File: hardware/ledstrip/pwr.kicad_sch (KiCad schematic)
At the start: 8 parts, among them J4 BMS connectors, J6 Header for STUSB4500 I2C, U5 BQ25703A, U6 STUSB4500QTR

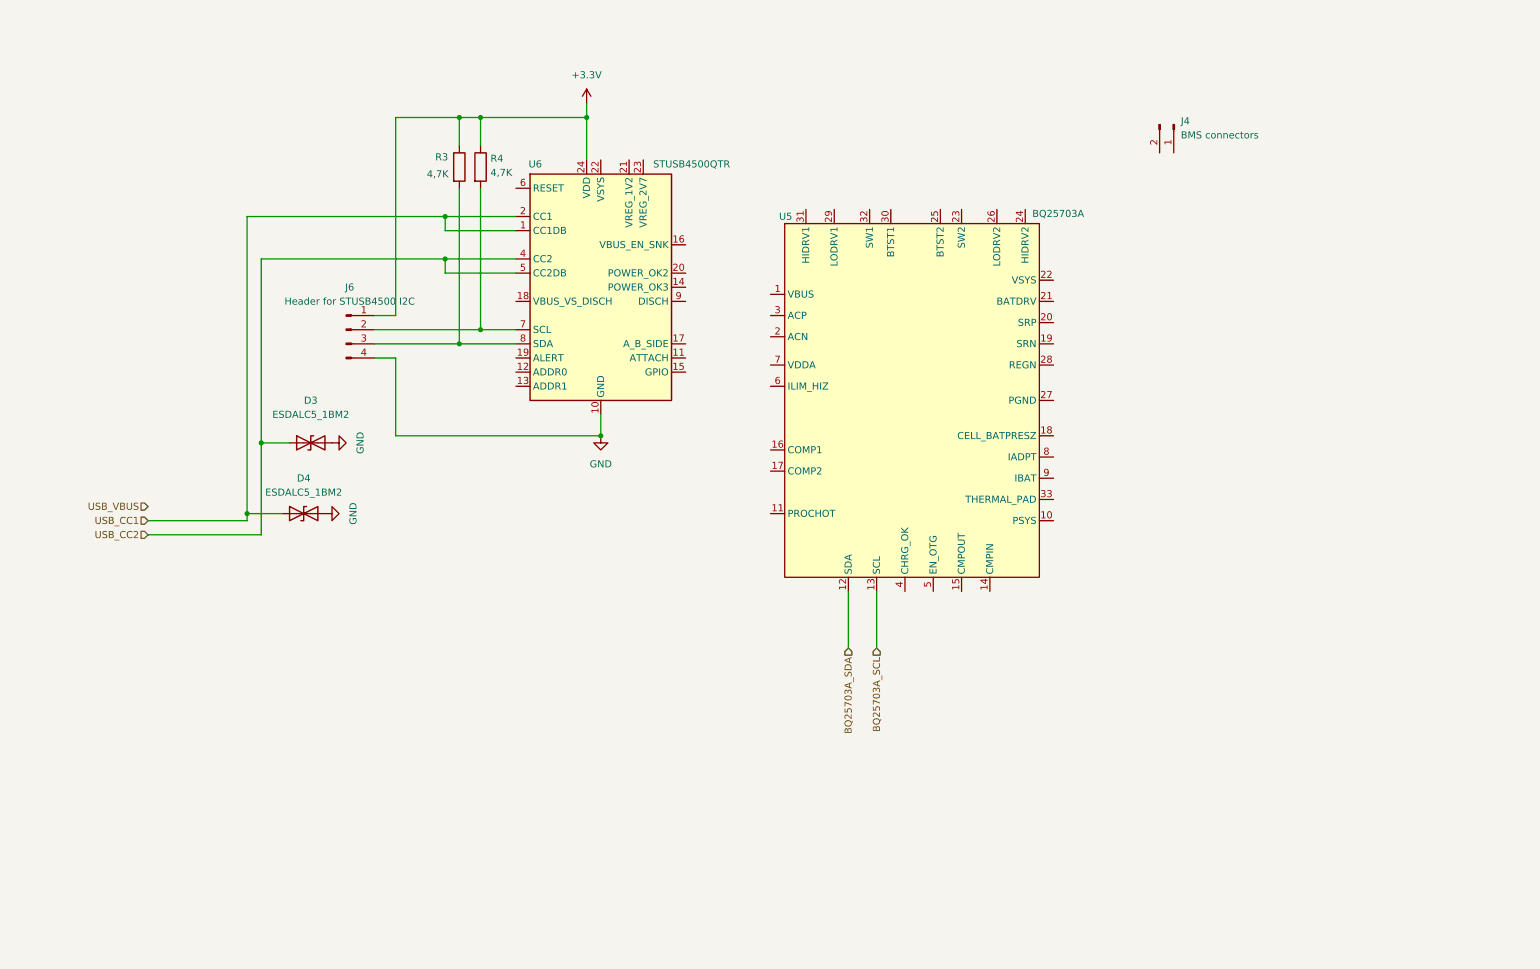
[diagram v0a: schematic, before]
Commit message: Add TVS diode on VBUS line, improve STUSB4500 integration
Add P-MOSFET controled by STUSB4500 on VBUS line
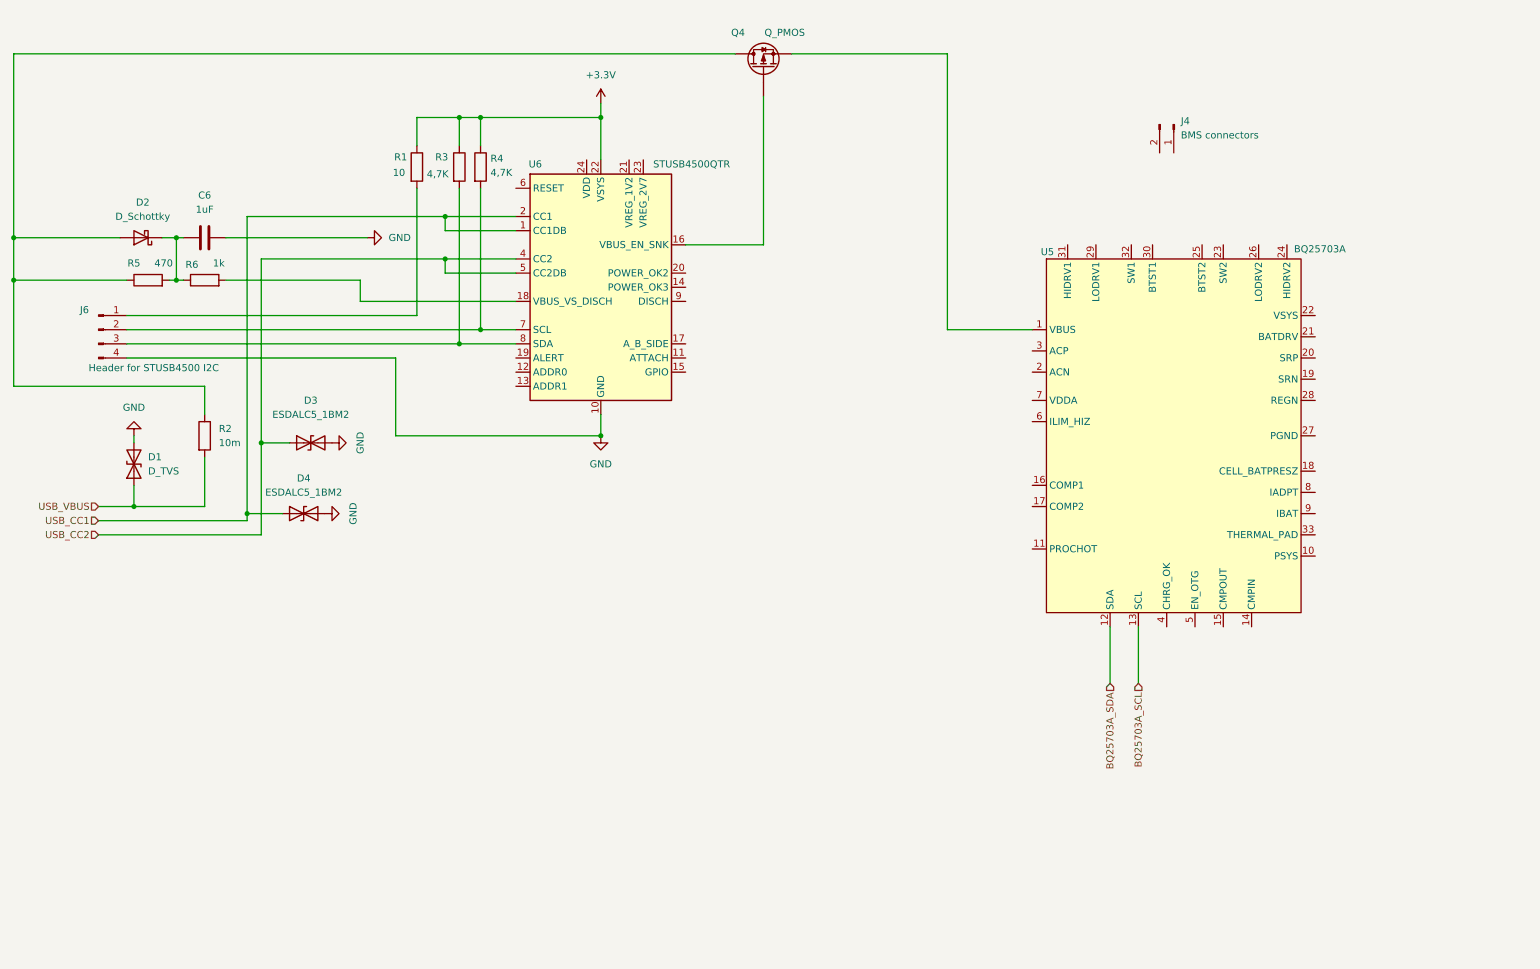
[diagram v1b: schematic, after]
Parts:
- added C6: 1uF, Capacitor_SMD:C_0603_1608Metric, symbol Device:C
- added D1: D_TVS, Diode_SMD:D_SMA, symbol Device:D_TVS
- added D2: D_Schottky, Diode_SMD:D_SOD-323, symbol Device:D_Schottky
- added Q4: Q_PMOS, symbol Device:Q_PMOS
- added R1: 10, Resistor_SMD:R_0805_2012Metric, symbol Device:R
- added R2: 10m, Resistor_SMD:R_0805_2012Metric, symbol Device:R
- added R5: 470, Capacitor_SMD:C_0603_1608Metric, symbol Device:R
- added R6: 1k, Capacitor_SMD:C_0603_1608Metric, symbol Device:R
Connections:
- net +3.3V: now also U6.22 (VSYS), R1.1; no longer J6.1 (Pin_1), U6.24 (VDD)
- net GND: now also C6.2, D1.2 (A2)
- net USB_VBUS: now also D1.1 (A1), R2.2
- net at U6.16 (VBUS_EN_SNK): now also Q4.G
- net at U6.18 (VBUS_VS_DISCH): now also R6.2
- net at U5.1 (VBUS): now also Q4.S
- new net: C6.1, D2.1 (K), R5.2, R6.1
- new net: J6.1 (Pin_1), R1.2
- new net: D2.2 (A), Q4.D, R2.1, R5.1
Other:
- moved on the sheet: J6, U5

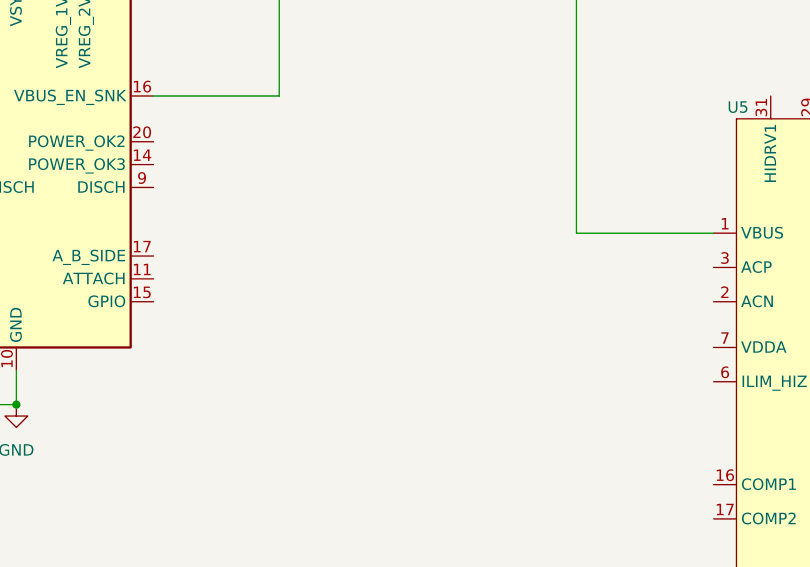
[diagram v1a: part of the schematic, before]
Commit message: Add STL6P3LLH6 sym from ulra librarian, add a TODO_plan_for_this_weekend.md for project organization
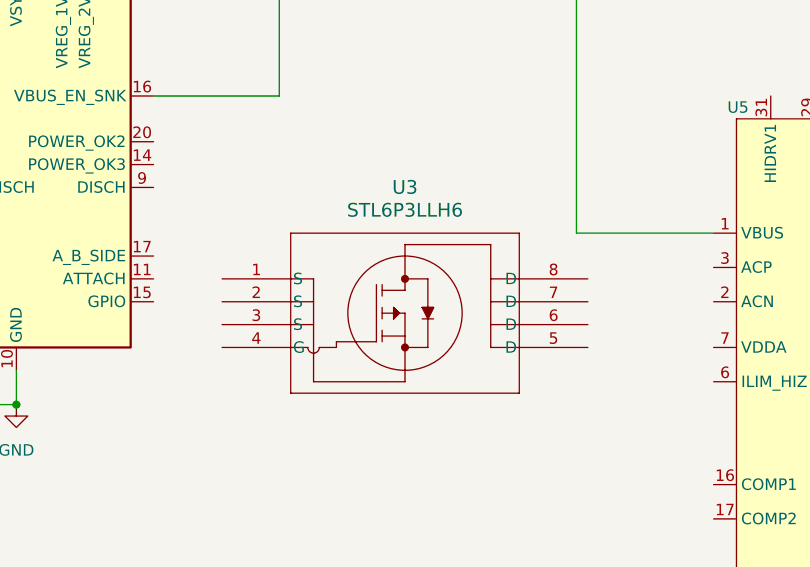
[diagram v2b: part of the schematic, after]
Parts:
- added U3: STL6P3LLH6, POWERFLAT_3P3X3P3_STM, symbol STL6P3LLH6:STL6P3LLH6
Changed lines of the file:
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@@
+	)
+	(symbol
+		(lib_id "STL6P3LLH6:STL6P3LLH6")
+		(at 142.24 72.39 0)
+		(unit 1)
+		(exclude_from_sim no)
+		(in_bom yes)
+		(on_board yes)
+		(dnp no)
+		(fields_autoplaced yes)
+		(property "Reference" "U3"
+			(at 162.56 62.23 0)
+			(effects
+				(font
+					(size 1.524 1.524)
+				)
+			)
+		)
+		(property "Value" "STL6P3LLH6"
+			(at 162.56 64.77 0)
+			(effects
+				(font
+					(size 1.524 1.524)
+				)
+			)
+		)
+		(property "Footprint" "POWERFLAT_3P3X3P3_STM"
+			(at 142.24 72.39 0)
+			(effects
+				(font
+					(size 1.27 1.27)
+					(italic yes)
+				)
+				(hide yes)
+			)
+		)
+		(property "Datasheet" "https://www.st.com/resource/en/datasheet/stl6p3llh6.pdf"
+			(at 142.24 72.39 0)
+			(effects
+				(font
+					(size 1.27 1.27)
+					(italic yes)
+				)
+				(hide yes)
+			)
+		)
+		(property "Description" ""
+			(at 142.24 72.39 0)
+			(effects
+				(font
+					(size 1.27 1.27)
+				)
+				(hide yes)
+			)
+		)
+		(pin "5"
+		)
+		(pin "6"
+		)
+		(pin "7"
+		)
+		(pin "8"
+		)
+		(pin "3"
+		)
+		(pin "2"
+		)
+		(pin "1"
+		)
+		(pin "4"
+		)
+		(instances
+			(project ""
+				(path "/dcb997ee-94c4-4df2-ba22-0e091735ddd7/b5cca531-fcff-4497-988a-ecdd56b3ddf9"
+					(reference "U3")
+					(unit 1)
+				)
+			)
+		)
 	)
 	(symbol

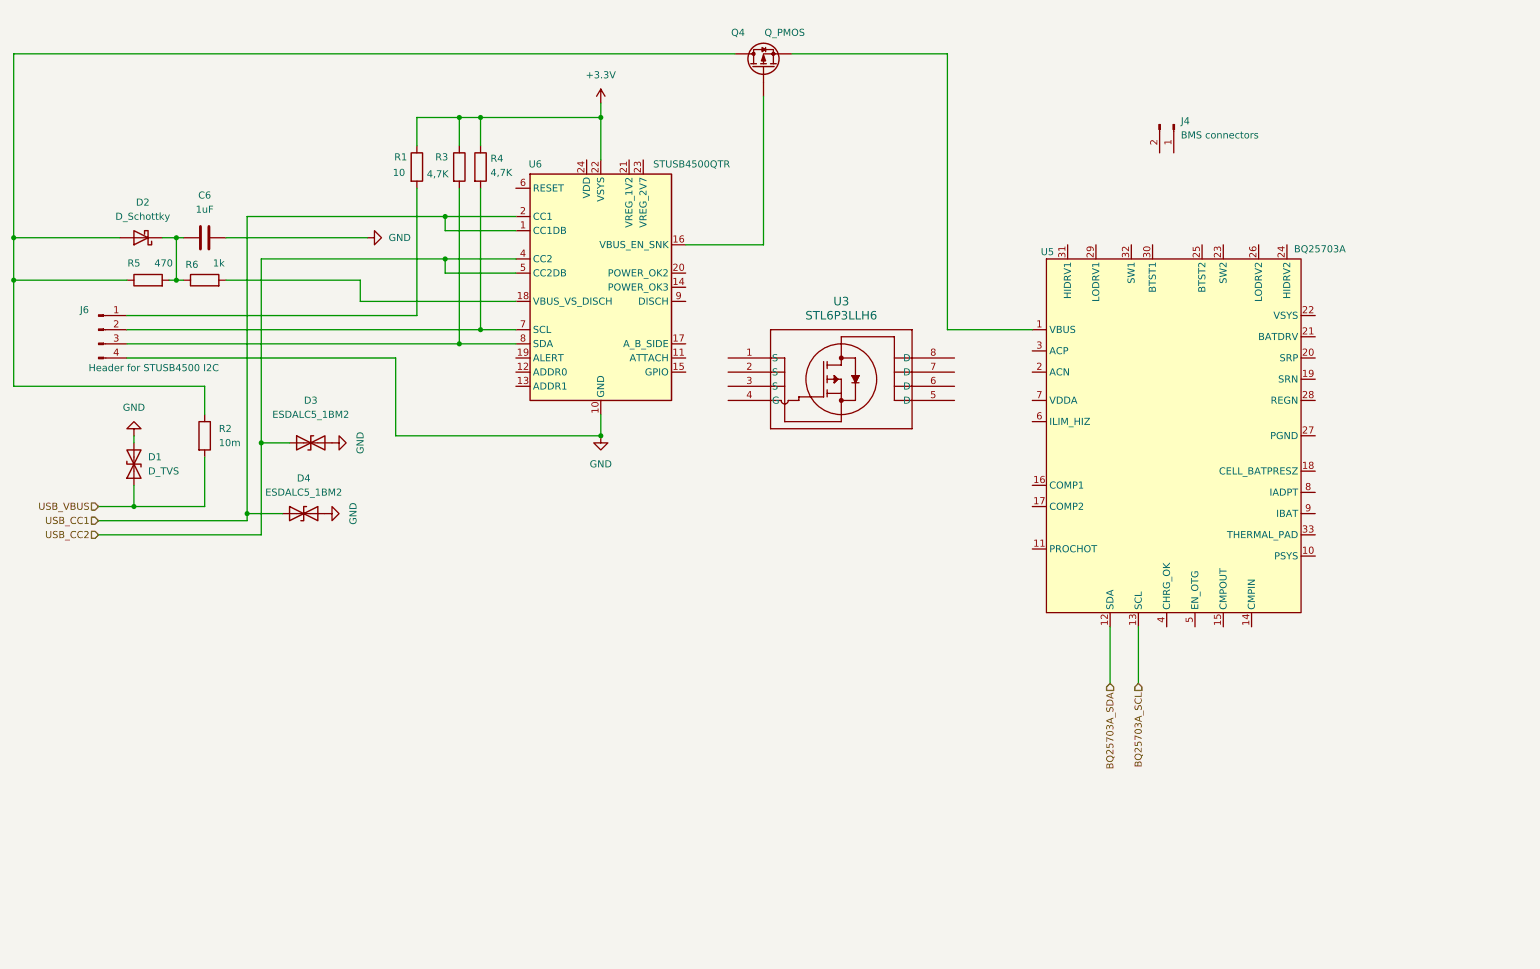
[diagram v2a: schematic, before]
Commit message: Finished STUSB4500 integration.
Improved BQ25703A integration.
Created a footprint for Wurth inductance.
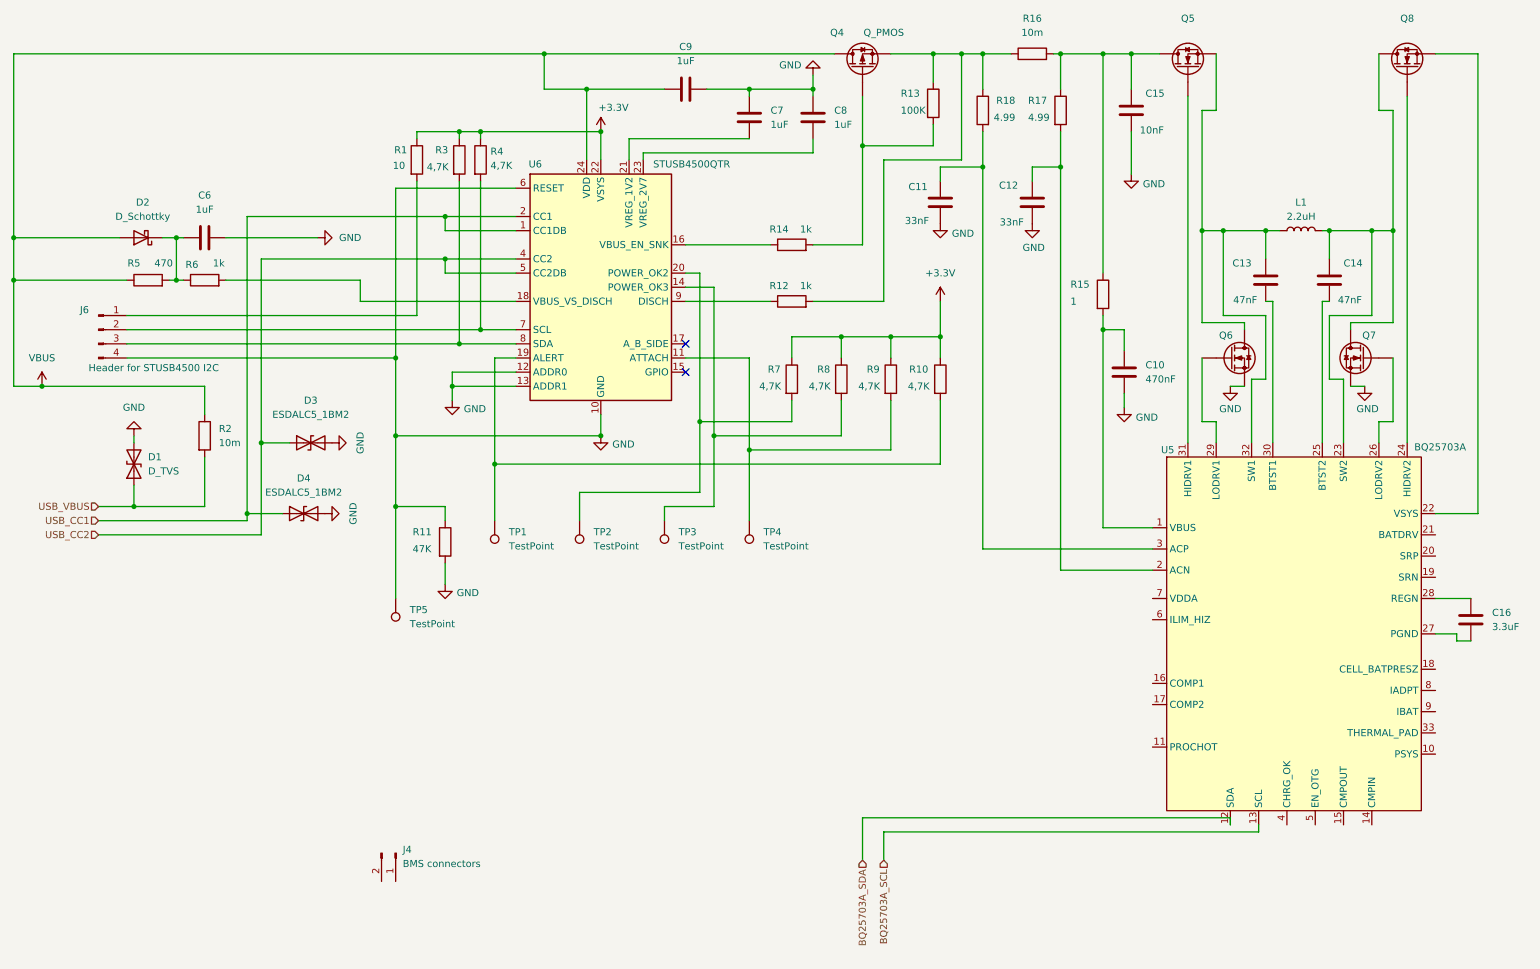
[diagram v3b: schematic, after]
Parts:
- removed U3: STL6P3LLH6, POWERFLAT_3P3X3P3_STM, symbol STL6P3LLH6:STL6P3LLH6
- added C10: 470nF, Capacitor_SMD:C_0603_1608Metric, symbol Device:C
- added C11, C12: 33nF, Capacitor_SMD:C_0603_1608Metric, symbol Device:C
- added C13, C14: 47nF, Capacitor_SMD:C_0603_1608Metric, symbol Device:C
- added C15: 10nF, Capacitor_SMD:C_0603_1608Metric, symbol Device:C
- added C16: 3.3uF, Capacitor_SMD:C_0603_1608Metric, symbol Device:C
- added C7, C8, C9: 1uF, Capacitor_SMD:C_0603_1608Metric, symbol Device:C
- added L1: 2.2uH, ledstrip:L_Wurth_WE-LHMI-8030_9.7x8.5mm, symbol Device:L
- added Q5, Q6, Q7, Q8: Q_NMOS, Package_SON:VSON-8_3.3x3.3mm_P0.65mm_NexFET, symbol Device:Q_NMOS
- added R10, R7, R8, R9: 4,7K, Resistor_SMD:R_0805_2012Metric, symbol Device:R
- added R11: 47K, Resistor_SMD:R_0805_2012Metric, symbol Device:R
- added R12, R14: 1k, Capacitor_SMD:C_0603_1608Metric, symbol Device:R
- added R13: 100K, Resistor_SMD:R_0805_2012Metric, symbol Device:R
- added R15: 1, Resistor_SMD:R_0805_2012Metric, symbol Device:R
- added R16: 10m, Resistor_SMD:R_0805_2012Metric, symbol Device:R
- added R17, R18: 4.99, Resistor_SMD:R_0805_2012Metric, symbol Device:R
- added TP1, TP2, TP3, TP4, TP5: TestPoint, symbol Connector:TestPoint
- Q4: footprint (none) -> STL6P3LLH6:POWERFLAT_3P3X3P3_STM
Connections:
- net +3.3V: now also R10.1, R7.1, R8.1, R9.1
- net GND: now also U6.12 (ADDR0), U6.13 (ADDR1), U6.6 (RESET), C10.1, C11.1, C12.1, C15.1, C7.2, C8.2, C9.2, Q6.S, Q7.S, R11.1, R11.2, TP5.1
- net VBUS: now reaches D2.2 (A), Q4.D, R2.1, R5.1
- net VBUS: now also U6.24 (VDD), C9.1
- net at Q4.G: now also R13.2, R14.2; no longer U6.16 (VBUS_EN_SNK)
- net at Q4.S: now also R12.2, R13.1, R16.1, R18.1; no longer U5.1 (VBUS)
- net at U6.11 (ATTACH): now also R9.2, TP4.1
- net at U6.14 (POWER_OK3): now also R8.2, TP3.1
- net at U6.19 (ALERT): now also R10.2, TP1.1
- net at U6.20 (POWER_OK2): now also R7.2, TP2.1
- net at U6.21 (VREG_1V2): now also C7.1
- net at U6.23 (VREG_2V7): now also C8.1
- net at U6.9 (DISCH): now also R12.1
- net at U5.2 (ACN): now also C12.2, R17.2
- net at U5.22 (VSYS): now also Q8.S
- net at U5.23 (SW2): now also C14.2, L1.2, Q7.D, Q8.D
- net at U5.24 (HIDRV2): now also Q8.G
- net at U5.25 (BTST2): now also C14.1
- net at U5.26 (LODRV2): now also Q7.G
- net at U5.27 (PGND): now also C16.1
- net at U5.28 (REGN): now also C16.2
- net at U5.29 (LODRV1): now also Q6.G
- net at U5.3 (ACP): now also C11.2, R18.2
- net at U5.30 (BTST1): now also C13.1
- net at U5.31 (HIDRV1): now also Q5.G
- net at U5.32 (SW1): now also C13.2, L1.1, Q5.S, Q6.D
- new net: C15.2, Q5.D, R15.1, R16.2, R17.1
- new net: C10.2, R15.2, U5.1 (VBUS)
- new net: R14.1, U6.16 (VBUS_EN_SNK)
- no-connect marks 0 -> 2
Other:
- moved on the sheet: J4, Q4, R1, R3, R4, U5
